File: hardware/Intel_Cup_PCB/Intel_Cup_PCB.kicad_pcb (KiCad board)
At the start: 2 copper layers, 75 x 110 mm, 20 parts, among them SW1 SW_SPST

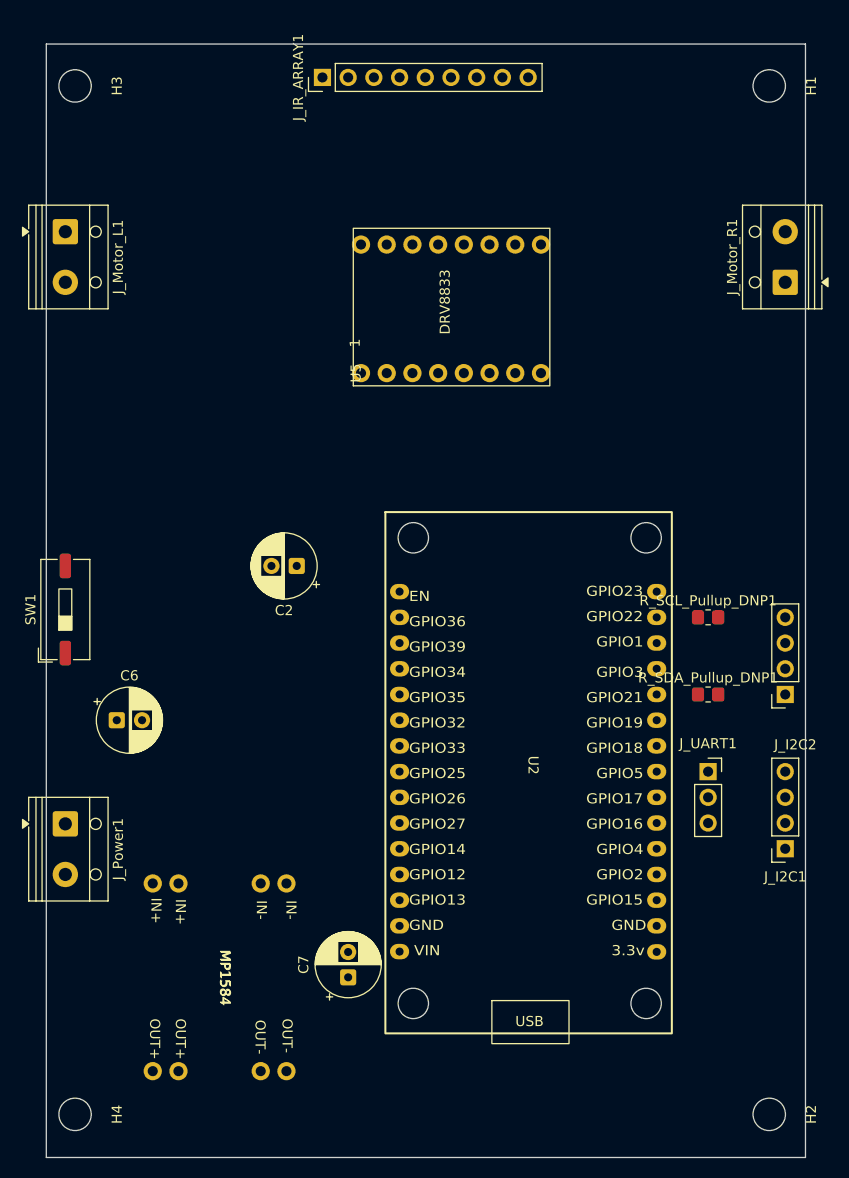
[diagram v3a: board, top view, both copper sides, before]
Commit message: Added ground plane
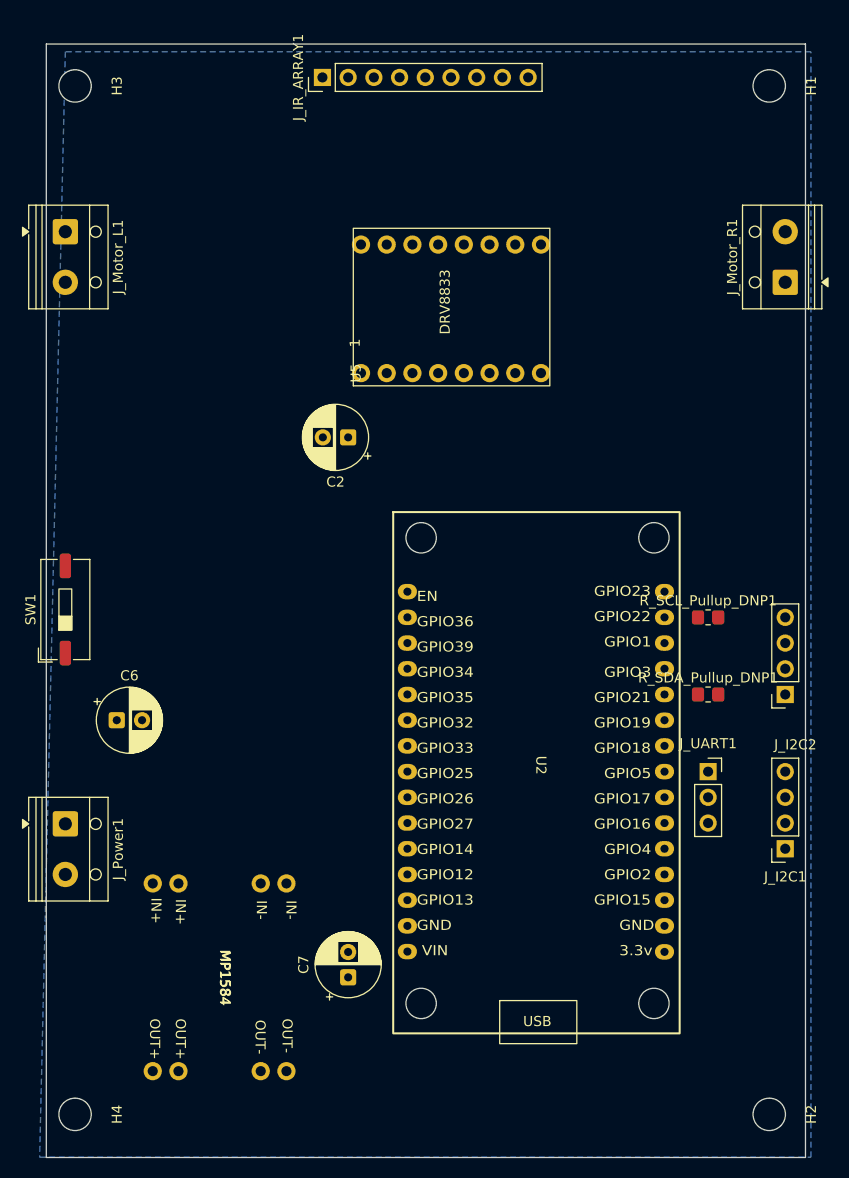
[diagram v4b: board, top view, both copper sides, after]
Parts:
- moved C2 13.7 mm to (147.3, 86.4)
- moved U2 0.77 mm to (165.1, 120.1)
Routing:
- added copper zone on B.Cu, net GND
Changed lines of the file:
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@@
 	)
 	(setup
+		(stackup
+			(layer "F.SilkS"
+				(type "Top Silk Screen")
+			)
+			(layer "F.Paste"
+				(type "Top Solder Paste")
+			)
+			(layer "F.Mask"
+				(type "Top Solder Mask")
+				(thickness 0.01)
+			)
+			(layer "F.Cu"
+				(type "copper")
+				(thickness 0.035)
+			)
+			(layer "dielectric 1"
+				(type "core")
+				(thickness 1.51)
+				(material "FR4")
+				(epsilon_r 4.5)
+				(loss_tangent 0.02)
+			)
+			(layer "B.Cu"
+				(type "copper")
+				(thickness 0.035)
+			)
+			(layer "B.Mask"
+				(type "Bottom Solder Mask")
+				(thickness 0.01)
+			)
+			(layer "B.Paste"
+				(type "Bottom Solder Paste")
+			)
+			(layer "B.SilkS"
+				(type "Bottom Silk Screen")
+			)
+			(copper_finish "None")
+			(dielectric_constraints no)
+		)
 		(pad_to_mask_clearance 0)
 		(allow_soldermask_bridges_in_footprints no)
@@
 		)
 		(property "Value" "4.7k"
-			(at -64.08 73.46 0)
+			(at 0 0 0)
 			(layer "F.Fab")
 			(effects
@@
 	(footprint "ESP32_Footprints:ESP32_30pin"
 		(layer "F.Cu")
-		(at 164.32754 120.140187)
+		(at 165.1 120.1402)
 		(property "Reference" "U2"
 			(at 1.27246 -1.395187 270)
@@
 	(footprint "Capacitor_THT:CP_Radial_D6.3mm_P2.50mm"
 		(layer "F.Cu")
-		(at 142.24 99.06 180)
+		(at 147.32 86.36 180)
 		(descr "CP, Radial series, Radial, pin pitch=2.50mm, diameter=6.3mm, height=7mm, Electrolytic Capacitor")
 		(tags "CP Radial series Radial pin pitch 2.50mm diameter 6.3mm height 7mm Electrolytic Capacitor")
@@
 		(layer "F.Cu")
 		(at 134.62 139.7 -90)
-		(property "Datasheet" ""
-			(at 0 0 270)
+		(property "Reference" "MP1584"
+			(at 0 -0.5 270)
 			(unlocked yes)
-			(layer "F.Fab")
-			(hide yes)
+			(layer "F.SilkS")
 			(effects
 				(font
 					(size 1 1)
-					(thickness 0.15)
+					(thickness 0.1)
 				)
 			)
 		)
-		(property "Description" ""
-			(at 0 0 270)
+		(property "Value" "~"
+			(at 0 1 270)
 			(unlocked yes)
 			(layer "F.Fab")
-			(hide yes)
 			(effects
 				(font
@@
 			)
 		)
-		(property "Value" "~"
-			(at 0 1 270)
+		(property "Datasheet" ""
+			(at 0 0 270)
 			(unlocked yes)
 			(layer "F.Fab")
+			(hide yes)
 			(effects
 				(font
@@
 			)
 		)
-		(property "Reference" "MP1584"
-			(at 0 -0.5 270)
+		(property "Description" ""
+			(at 0 0 270)
 			(unlocked yes)
-			(layer "F.SilkS")
+			(layer "F.Fab")
+			(hide yes)
 			(effects
 				(font
 					(size 1 1)
-					(thickness 0.1)
+					(thickness 0.15)
 				)
 			)
@@
 		(layer "Edge.Cuts")
 	)
+	(zone
+		(net "GND")
+		(layer "B.Cu")
+		(hatch edge 0.5)
+		(connect_pads
+			(clearance 0.5)
+		)
+		(min_thickness 0.25)
+		(fill yes
+			(thermal_gap 0.5)
+			(thermal_bridge_width 0.5)
+			(island_removal_mode 0)
+		)
+		(polygon
+			(pts
+				(xy 119.38 48.26) (xy 116.84 157.48) (xy 193.04 157.48) (xy 193.04 48.26)
+			)
+		)
+	)
 	(embedded_fonts no)

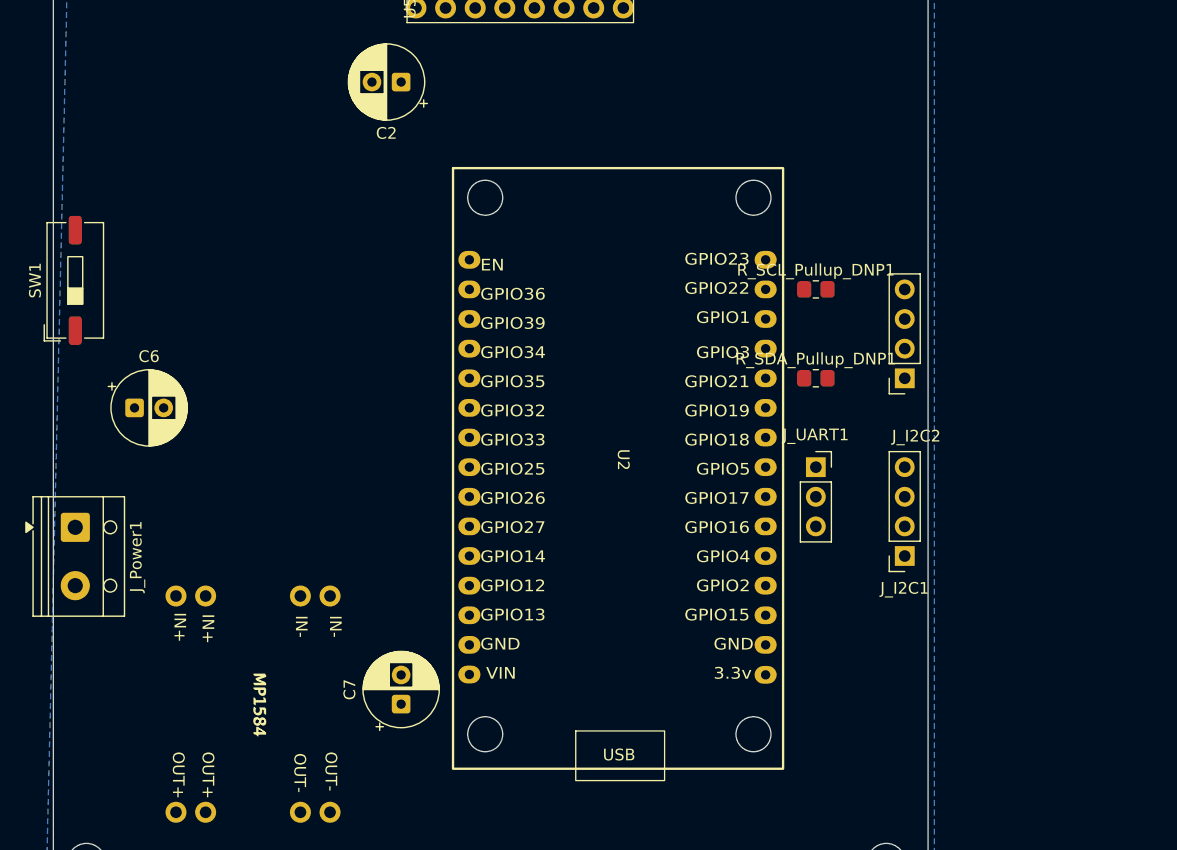
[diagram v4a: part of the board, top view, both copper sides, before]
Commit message: Added new nets for MP1584 and fixed footprints
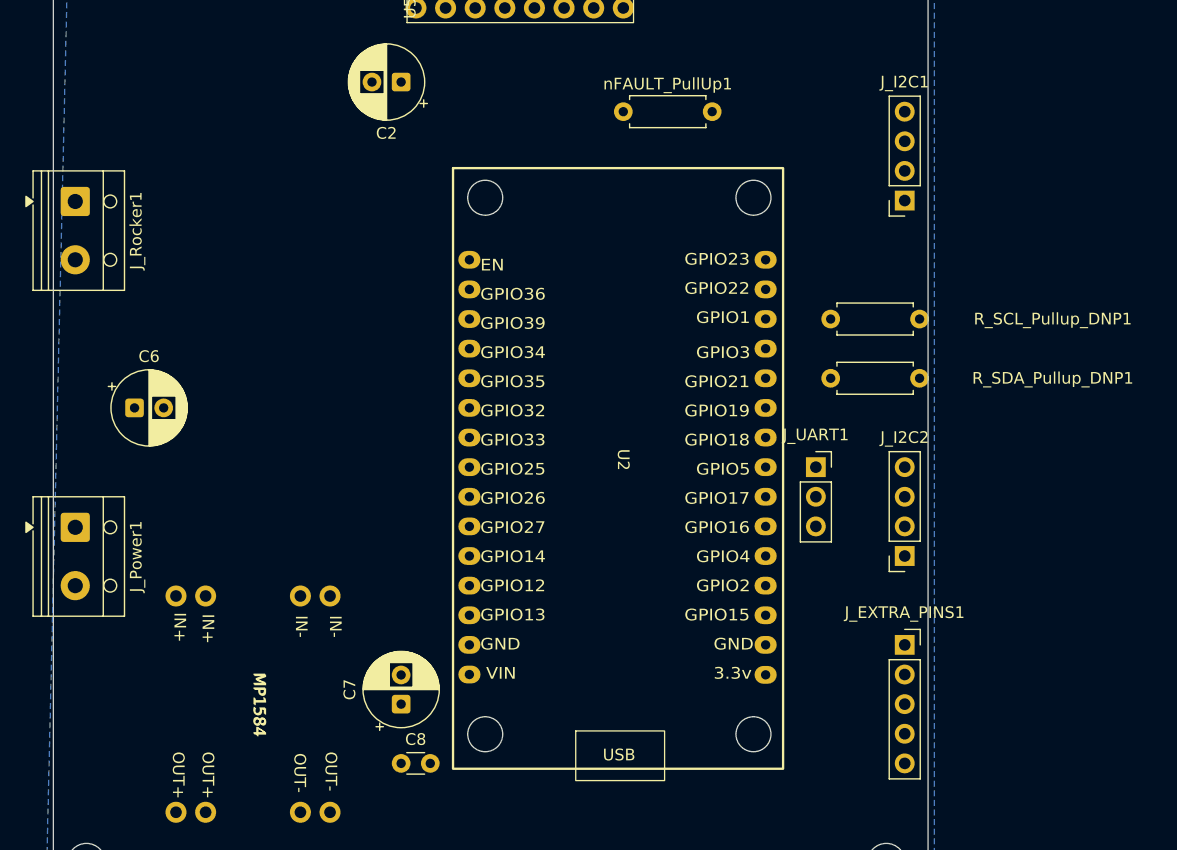
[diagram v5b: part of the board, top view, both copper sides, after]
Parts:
- removed SW1: SW_SPST, Button_Switch_SMD:SW_DIP_SPSTx01_Slide_9.78x4.72mm_W8.61mm_P2.54mm
- added C8: 0.1uF, Capacitor_THT:C_Disc_D3.0mm_W1.6mm_P2.50mm, F.Cu at (147.3, 144.8)
- added J_EXTRA_PINS1: Conn_01x05_Pin, Connector_PinSocket_2.54mm:PinSocket_1x05_P2.54mm_Vertical, F.Cu at (190.5, 134.6)
- added J_Rocker1: Conn_01x02_Pin, TerminalBlock_RND:TerminalBlock_RND_205-00012_1x02_P5.00mm_Horizontal, F.Cu at (119.4, 96.6)
- added nFAULT_PullUp1: 10k, Resistor_THT:R_Axial_DIN0207_L6.3mm_D2.5mm_P7.62mm_Horizontal, F.Cu at (166.4, 88.9)
- R_SCL_Pullup_DNP1, R_SDA_Pullup_DNP1: footprint Resistor_SMD:R_0805_2012Metric_Pad1.20x1.40mm_HandSolder -> Resistor_THT:R_Axial_DIN0207_L6.3mm_D2.5mm_P7.62mm_Horizontal
- moved J_I2C2 15.2 mm to (190.5, 96.5)
- moved R_SCL_Pullup_DNP1 2.84 mm to (184.2, 106.7)
- moved R_SDA_Pullup_DNP1 1.27 mm to (184.2, 111.8)
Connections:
- C2 pad 1: GND -> VBAT_MOT
- C2 pad 2: VBAT_MOT -> GND
- C7 pad 1: GND -> +5V_ESP
- C7 pad 2: +5V_ESP -> GND
- J_IR_ARRAY1 pad 1: /IO32 -> /IO4
- J_IR_ARRAY1 pad 2: /IO35 -> /IO5
- J_IR_ARRAY1 pad 3: /IO34 -> /IO18
- J_IR_ARRAY1 pad 4: /IO39 -> /IO19
- J_IR_ARRAY1 pad 5: /IO36 -> /IO23
- J_IR_ARRAY1 pad 6: /CTRL_ODD -> /IO32
- J_IR_ARRAY1 pad 7: /CTRL_EVEN -> /IO33
- MP1584 pad 1: (no net) -> GND
- MP1584 pad 2: (no net) -> unconnected-(MP1584-IN--Pad2)
- MP1584 pad 3: (no net) -> VBAT_MOT
- MP1584 pad 4: (no net) -> unconnected-(MP1584-IN+-Pad4)
- MP1584 pad 5: (no net) -> GND
- MP1584 pad 6: (no net) -> unconnected-(MP1584-OUT--Pad6)
- MP1584 pad 7: (no net) -> +5V_ESP
- MP1584 pad 8: (no net) -> unconnected-(MP1584-OUT+-Pad8)
- U5 pad 8: /IO33 -> /IO35

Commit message: Updated footprints
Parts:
- moved C6 38.1 mm to (147.3, 83.8), turned to 180 degrees
- moved C2 19.8 mm to (132.1, 99.1)
- moved J_Rocker1 17.7 mm to (119.4, 114.3), turned to 90 degrees
- moved MP1584 15.7 mm to (141.1, 125.4)
- moved C7 2.58 mm to (147.3, 137.1)
- moved R_SCL_Pullup_DNP1 2.54 mm to (184.2, 104.1)
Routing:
- added copper zone on F.Cu, net GND

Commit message: Minor fixes
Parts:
- ESP32_Devkit1: renamed from U2; value ~ -> ESP32_Devkit1
- MP1584: value ~ -> MP1584
- moved C2 18.5 mm to (137.1, 116.8)
- moved MP1584 9.91 mm to (141.5, 135.3)
- moved R_SCL_Pullup_DNP1 7.43 mm to (191.1, 106.7), turned to 180 degrees
- moved R_SDA_Pullup_DNP1 6.35 mm to (190.5, 111.8), turned to 180 degrees
- moved J_Motor_R1 5.61 mm to (188.0, 66.0), turned to -90 degrees
- moved C6 3.59 mm to (144.8, 81.3)
- moved J_Rocker1 3.34 mm to (122.7, 114.3)
- moved J_Power1 3.18 mm to (122.6, 124.5)
- moved J_Motor_L1 3.01 mm to (122.4, 66.1)
- moved C7 2.01 mm to (148.0, 139.0)
- moved H4 0.94 mm to (121.3, 153.2)
- moved J_I2C1 0.63 mm to (189.9, 127.0)
- moved J_I2C2 0.63 mm to (189.9, 96.5)
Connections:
- J_EXTRA_PINS1 pad 1: /IO4 -> /IO34
- J_EXTRA_PINS1 pad 2: /IO5 -> /IO36
- J_EXTRA_PINS1 pad 3: /IO18 -> /IO39
- J_EXTRA_PINS1 pad 4: /IO19 -> /IO12(BOOT)
- J_EXTRA_PINS1 pad 5: /IO23 -> /IO15(BOOT)
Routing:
- net /IO18: track 0.00 -> 165.9 mm
- net /IO4: track 0.00 -> 129.9 mm, vias 0 -> 6
- net +3.3V: track 0.00 -> 115.1 mm, vias 0 -> 1
- net /IO5: track 0.00 -> 105.6 mm, vias 0 -> 2
- net /IO19: track 0.00 -> 99.1 mm, vias 0 -> 2
- net /IO33: track 0.00 -> 94.2 mm, vias 0 -> 1
- net GND: track 0.00 -> 91.4 mm, vias 0 -> 14
- net /IO32: track 0.00 -> 89.8 mm
- net VBAT_MOT: track 0.00 -> 89.1 mm
- net /IO13: track 0.00 -> 84.3 mm, vias 0 -> 2
- net /IO23: track 0.00 -> 77.7 mm, vias 0 -> 2
- net /IO39: track 0.00 -> 58.8 mm, vias 0 -> 4
- net /IO34: track 0.00 -> 58.0 mm
- net /IO14: track 0.00 -> 56.5 mm
- net /IO27: track 0.00 -> 53.9 mm
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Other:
- board text added: "IO12"
- board text added: "IO15"
- board text added: "IO34"
- board text added: "IO36"
- board text added: "IO39"

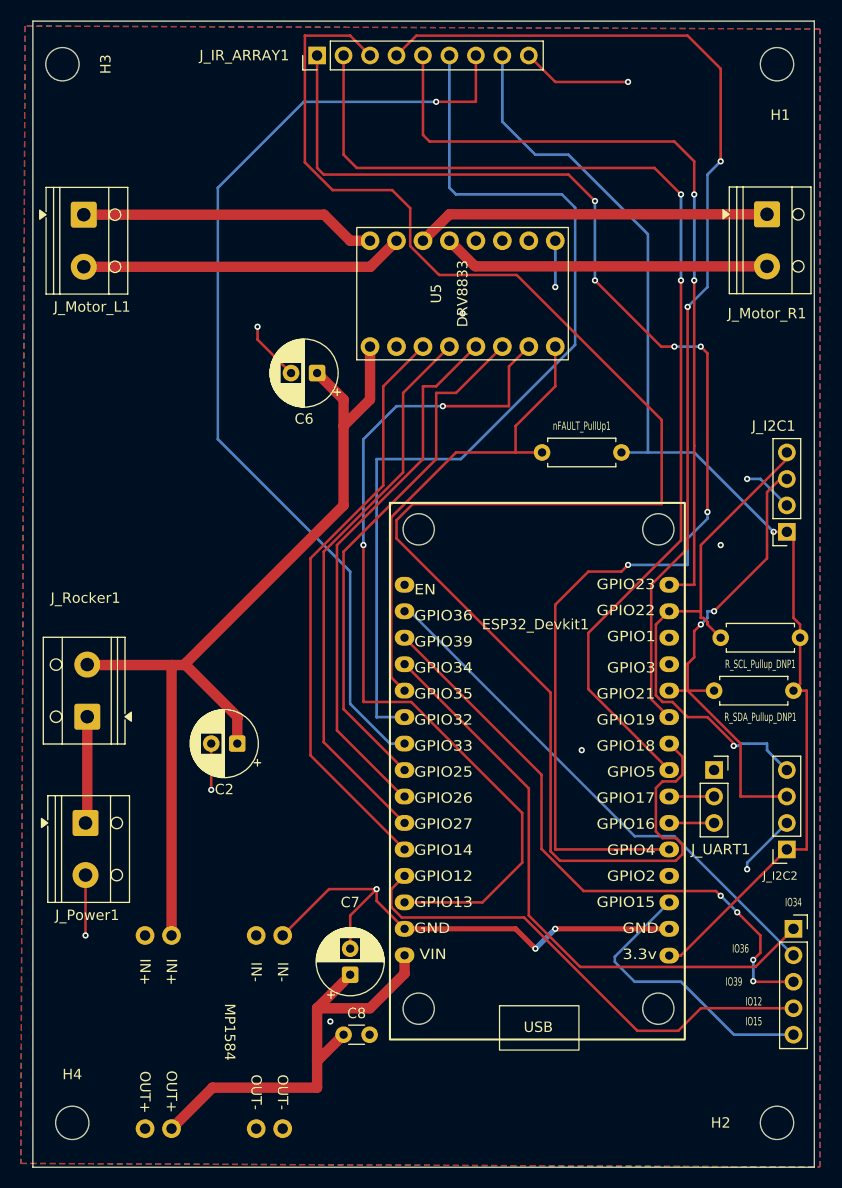
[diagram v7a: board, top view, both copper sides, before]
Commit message: Added bump sensor and distance sensor footprints
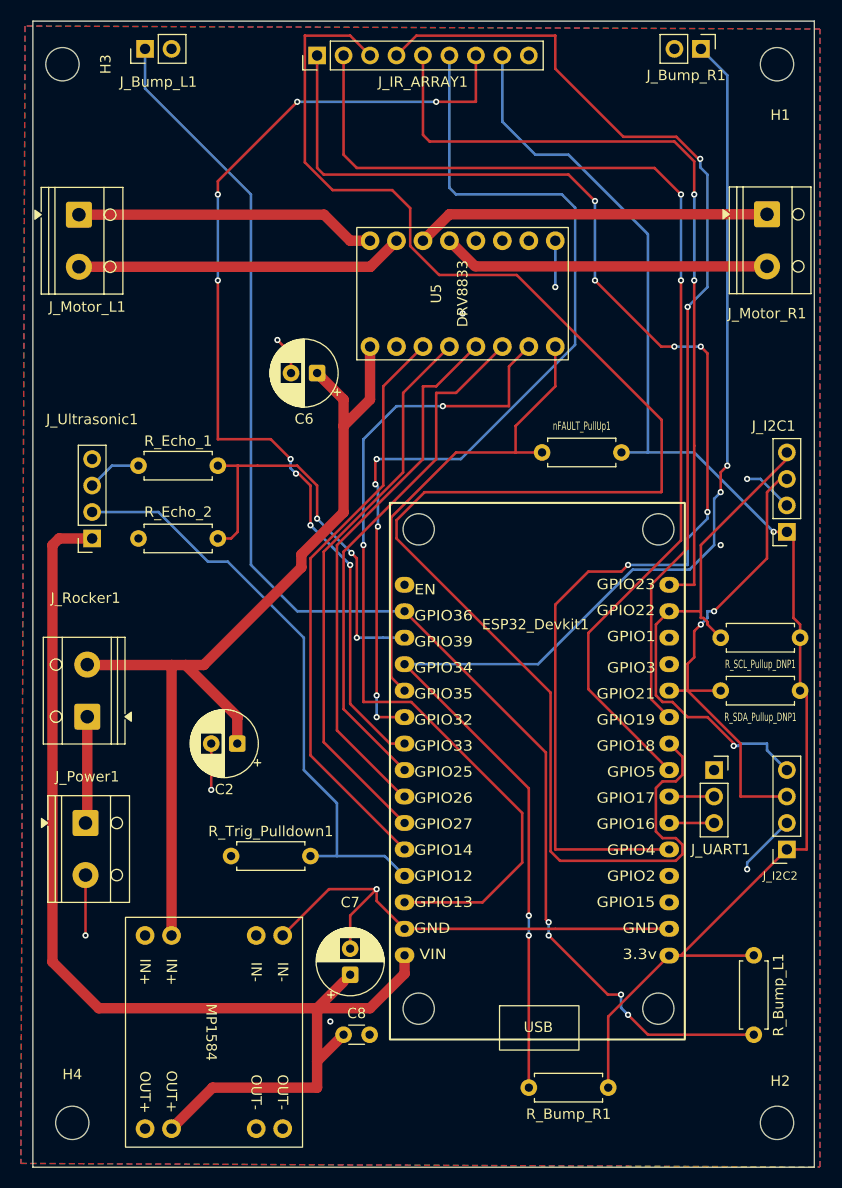
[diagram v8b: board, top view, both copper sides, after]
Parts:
- removed J_EXTRA_PINS1: Conn_01x05_Pin, Connector_PinSocket_2.54mm:PinSocket_1x05_P2.54mm_Vertical
- added J_Bump_L1: Conn_01x02_Pin, Connector_PinHeader_2.54mm:PinHeader_1x02_P2.54mm_Vertical, F.Cu at (128.3, 50.2)
- added J_Bump_R1: Conn_01x02_Pin, Connector_PinHeader_2.54mm:PinHeader_1x02_P2.54mm_Vertical, F.Cu at (181.6, 50.2)
- added J_Ultrasonic1: ~, Connector_PinSocket_2.54mm:PinSocket_1x04_P2.54mm_Vertical, F.Cu at (123.2, 97.2)
- added R_Bump_L1: 10k, Resistor_THT:R_Axial_DIN0207_L6.3mm_D2.5mm_P7.62mm_Horizontal, F.Cu at (186.7, 137.2)
- added R_Bump_R1: 10k, Resistor_THT:R_Axial_DIN0207_L6.3mm_D2.5mm_P7.62mm_Horizontal, F.Cu at (172.7, 149.9)
- added R_Echo_1: 10k, Resistor_THT:R_Axial_DIN0207_L6.3mm_D2.5mm_P7.62mm_Horizontal, F.Cu at (127.6, 90.2)
- added R_Echo_2: 20k, Resistor_THT:R_Axial_DIN0207_L6.3mm_D2.5mm_P7.62mm_Horizontal, F.Cu at (135.3, 97.2)
- added R_Trig_Pulldown1: 10k, Resistor_THT:R_Axial_DIN0207_L6.3mm_D2.5mm_P7.62mm_Horizontal, F.Cu at (136.5, 127.6)
- ESP32_Devkit1: value ESP32_Devkit1 -> ~
- moved R_SDA_Pullup_DNP1 0.63 mm to (191.1, 111.8)
- moved J_Motor_L1 0.47 mm to (121.9, 66.1)
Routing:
- net /IO36: track 51.0 -> 132.0 mm, vias 0 -> 4
- net +5V_ESP: track 41.9 -> 113.3 mm
- net /IO34: track 58.0 -> 129.2 mm, vias 0 -> 4
- net /IO15(BOOT): track 27.9 -> 0.00 mm
- net +3.3V: track 115.1 -> 138.3 mm
- net /IO39: track 58.8 -> 39.6 mm, vias 4 -> 3
- net GND: track 91.4 -> 77.2 mm, vias 14 -> 10
- net /IO12(BOOT): track 47.9 -> 57.4 mm
- net /IO19: track 99.1 -> 93.7 mm
- net Net-(J_Ultrasonic1-Pin_3): track 0.00 -> 5.23 mm
- net /IO33: track 94.2 -> 97.8 mm, vias 1 -> 8
- net VBAT_MOT: track 89.1 -> 90.1 mm
- net /IO18: track 165.9 -> 165.2 mm
- net /IO32: track 89.8 -> 90.0 mm, vias 0 -> 5
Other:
- board text added: "R_Echo_2"
- board text removed: "IO12"
- board text removed: "IO15"
- board text removed: "IO34"
- board text removed: "IO36"
- board text removed: "IO39"
